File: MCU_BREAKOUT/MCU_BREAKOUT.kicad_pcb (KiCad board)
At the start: 4 copper layers, 15 parts, among them J1 Conn_01x06_Pin, J10 Conn_01x03_Pin, J2 Conn_01x02_Pin, J3 Conn_01x02_Pin, J4 Conn_01x04_Pin, J5 Conn_01x02_Pin, J6 Conn_01x02_Pin, J7 Conn_01x02_Pin, J8 Conn_01x03_Pin, J9 Conn_01x04_Pin, U1 ATMEGA168PA-MU, U2 XL7EL89CKI-111YLC-16M

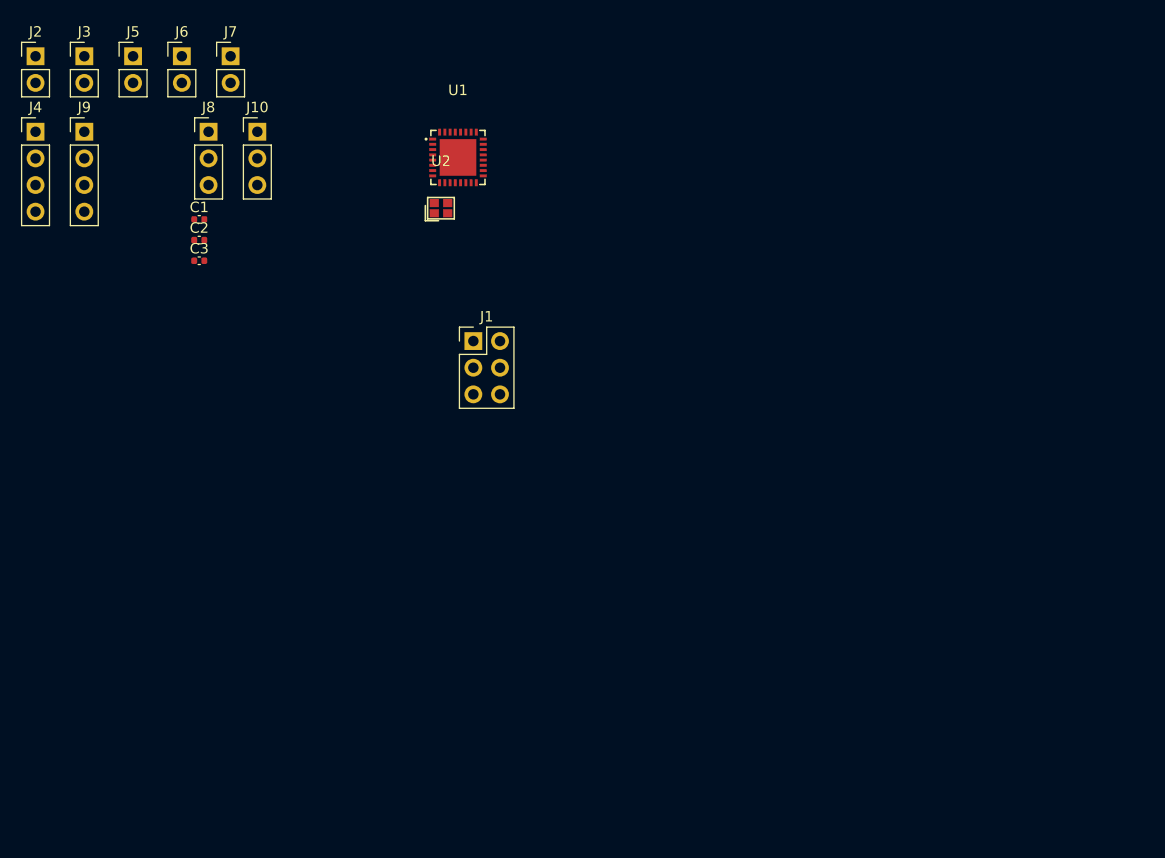
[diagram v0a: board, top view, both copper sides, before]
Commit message: RTC and GPS Breakouts Finished
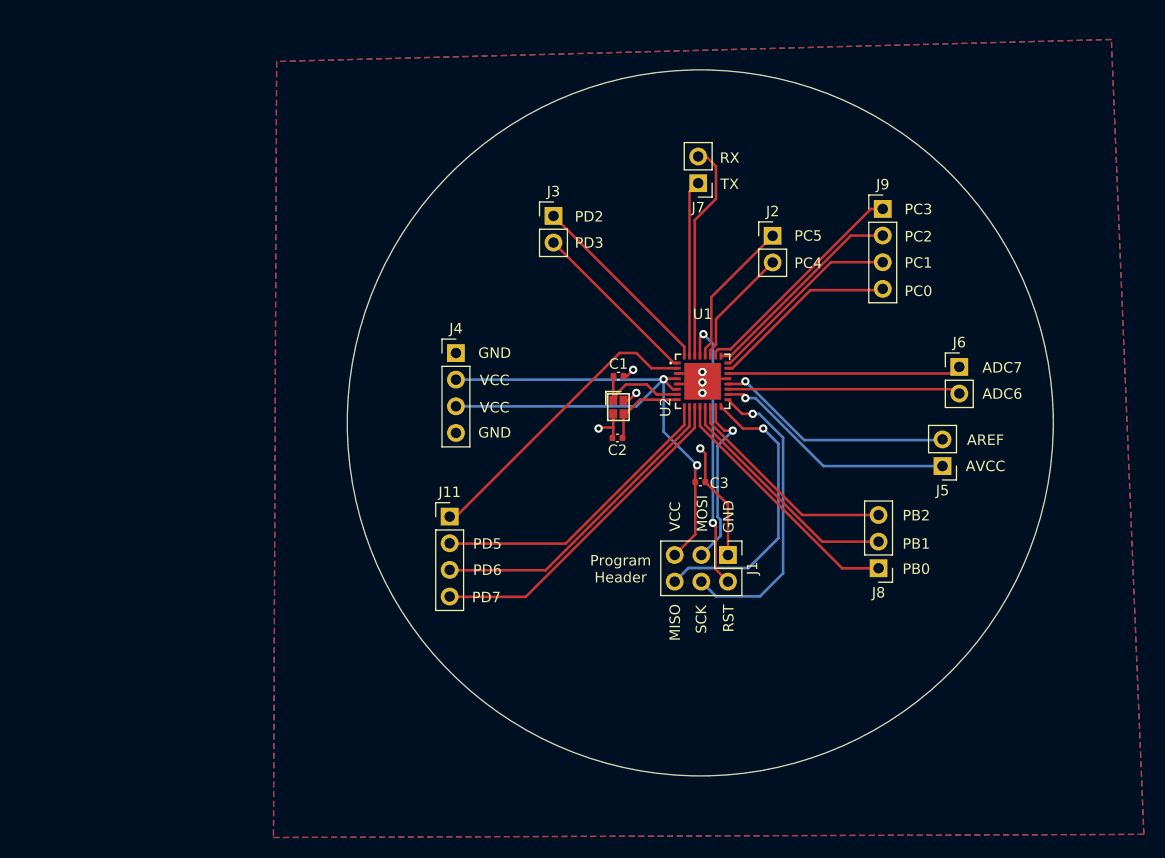
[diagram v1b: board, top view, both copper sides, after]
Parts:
- removed J10: Conn_01x03_Pin, Connector_PinHeader_2.54mm:PinHeader_1x03_P2.54mm_Vertical
- added J11: Conn_01x04_Pin, Connector_PinHeader_2.54mm:PinHeader_1x04_P2.54mm_Vertical, F.Cu at (143.0, 106.5)
- moved J5 86.5 mm to (190.0, 101.7), turned to 180 degrees
- moved J6 79.8 mm to (191.6, 92.2)
- moved J9 76.5 mm to (184.3, 77.2)
- moved J8 76.3 mm to (183.9, 111.4), turned to 180 degrees
- moved J2 72.3 mm to (173.8, 79.7)
- moved C3 52.2 mm to (166.9, 103.2), turned to 180 degrees
- moved J3 47.3 mm to (152.9, 77.8)
- moved J7 46.2 mm to (166.7, 74.7), turned to 180 degrees
- moved J4 45.3 mm to (143.6, 90.9)
- moved C2 44.1 mm to (159.0, 99.0), turned to 180 degrees
- moved C1 42.7 mm to (159.1, 93.1)
- moved J1 31.7 mm to (169.5, 110.2), turned to -90 degrees
- moved U1 31.6 mm to (167.1, 93.6)
- moved U2 25.4 mm to (159.1, 96.1), turned to -90 degrees
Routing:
- net VCC: track 0.00 -> 62.7 mm, vias 0 -> 2
- net /PD7: track 0.00 -> 32.1 mm
- net /PD6: track 0.00 -> 30.4 mm
- net /PB5: track 0.00 -> 29.0 mm, vias 0 -> 1
- net /PD5: track 0.00 -> 28.8 mm
- net /PD4: track 0.00 -> 28.8 mm
- net /PB4: track 0.00 -> 27.6 mm, vias 0 -> 1
- net /PC6: track 0.00 -> 26.8 mm, vias 0 -> 2
- net GND: track 0.00 -> 25.9 mm, vias 0 -> 7
- net /PB0: track 0.00 -> 24.5 mm
- net /AVCC: track 0.00 -> 23.6 mm, vias 0 -> 1
- net /AREF: track 0.00 -> 23.0 mm, vias 0 -> 1
- net /PB1: track 0.00 -> 22.9 mm
- net /ADC7: track 0.00 -> 22.3 mm
- net /ADC6: track 0.00 -> 22.2 mm
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- added copper zone on B.Cu, net GND
- added copper zone on F.Cu, net GND
- added copper zone on In1.Cu, net GND
- added copper zone on In2.Cu, net GND
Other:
- board outline added: 67.3 x 67.3 mm
- board text added: "ADC6"
- board text added: "ADC7"
- board text added: "AREF"
- board text added: "AVCC"
- board text added: "GND"
- board text added: "MISO"
- board text added: "MOSI"
- board text added: "PB0"
- board text added: "PB1"
- board text added: "PB2"
- board text added: "PC0"
- board text added: "PC1"
- board text added: "PC2"
- board text added: "PC3"
- board text added: "PC4"
- board text added: "PC5"
- board text added: "PD2"
- board text added: "PD3"
- board text added: "PD5"
- board text added: "PD6"
- board text added: "PD7"
- board text added: "Program Header"
- board text added: "RST"
- board text added: "RX"
- board text added: "SCK"
- board text added: "TX"
- board text added: "VCC"

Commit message: Added footprints and finished breakouts
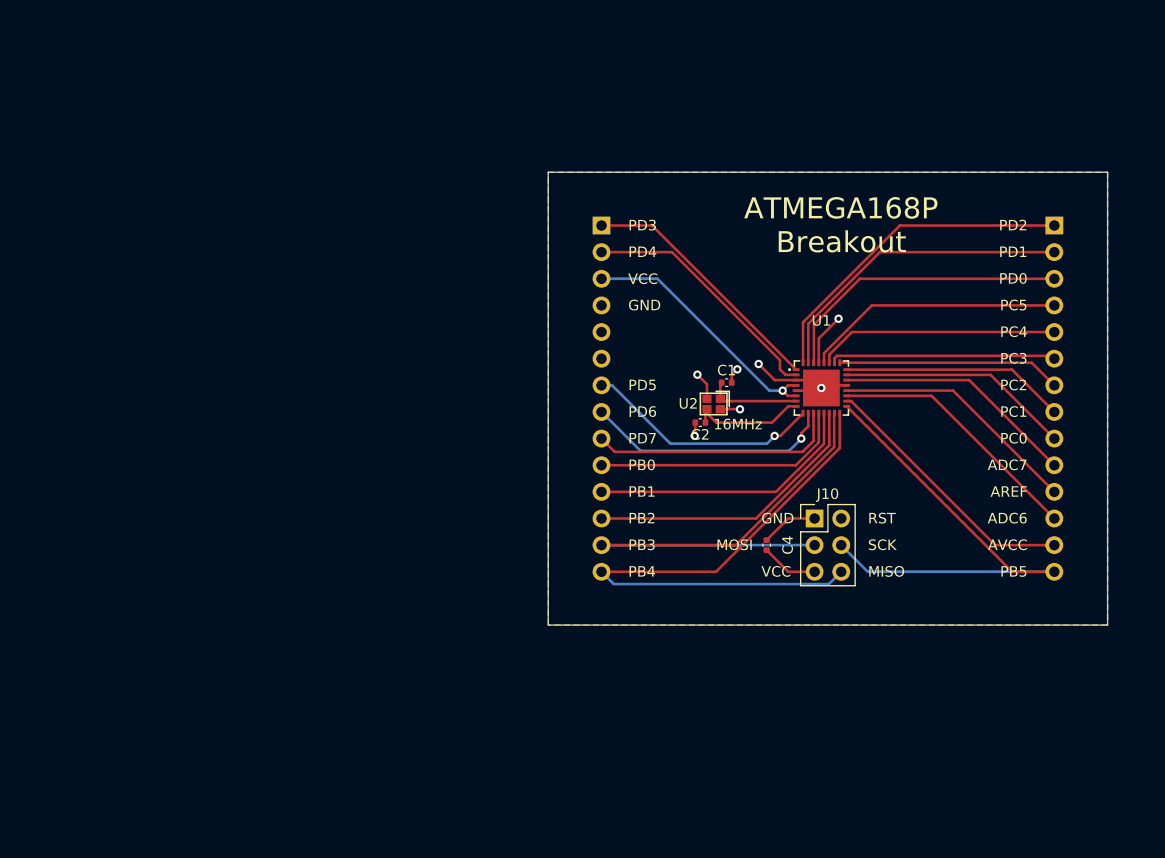
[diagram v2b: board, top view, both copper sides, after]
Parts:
- removed C3: 100n, Capacitor_SMD:C_0402_1005Metric
- removed J11, J4, J9: Conn_01x04_Pin, Connector_PinHeader_2.54mm:PinHeader_1x04_P2.54mm_Vertical
- removed J3, J5, J6, J7: Conn_01x02_Pin, Connector_PinHeader_2.54mm:PinHeader_1x02_P2.54mm_Vertical
- removed J8: Conn_01x03_Pin, Connector_PinHeader_2.54mm:PinHeader_1x03_P2.54mm_Vertical
- added C4: 100n, Capacitor_SMD:C_0402_1005Metric, F.Cu at (173.2, 109.2)
- added J10: Conn_01x06_Pin, Connector_PinHeader_2.54mm:PinHeader_2x03_P2.54mm_Vertical, F.Cu at (177.8, 106.7)
- J1: value Conn_01x06_Pin -> Conn_01x14_Pin; footprint Connector_PinHeader_2.54mm:PinHeader_2x03_P2.54mm_Vertical -> Connector_PinHeader_2.54mm:PinHeader_1x14_P2.54mm_Vertical; moved to B.Cu
- J2: value Conn_01x02_Pin -> Conn_01x14_Pin; footprint Connector_PinHeader_2.54mm:PinHeader_1x02_P2.54mm_Vertical -> Connector_PinHeader_2.54mm:PinHeader_1x14_P2.54mm_Vertical; moved to B.Cu
- moved J1 44.2 mm to (200.7, 78.7), turned to 180 degrees
- moved J2 16.3 mm to (157.5, 78.7), turned to 180 degrees
- moved U1 11.3 mm to (178.4, 94.2)
- moved C1 10.3 mm to (169.4, 93.7)
- moved U2 9.09 mm to (168.2, 95.8), turned to 180 degrees
- moved C2 8.04 mm to (166.9, 97.5)
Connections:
- J1 pad 1: GND -> /PD2
- J1 pad 2: /PC6 -> /PD1
- J1 pad 3: /PB3 -> /PD0
- J1 pad 4: /PB5 -> /PC5
- J1 pad 5: VCC -> /PC4
- J1 pad 6: /PB4 -> /PC3
- J2 pad 1: /PC5 -> /PD3
- J2 pad 2: /PC4 -> /PD4
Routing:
- net /PB3: track 16.8 -> 49.6 mm, vias 1 -> 0
- net /PB4: track 27.6 -> 54.8 mm, vias 1 -> 0
- net /PB5: track 29.0 -> 47.7 mm, vias 1 -> 0
- net VCC: track 62.7 -> 48.7 mm, vias 2 -> 1
- net /PD1: track 16.8 -> 30.0 mm
- net /PD2: track 18.5 -> 31.6 mm
- net /PC4: track 11.4 -> 23.1 mm
- net /PC5: track 14.1 -> 24.8 mm
- net /PD7: track 32.1 -> 23.8 mm
- net /PD3: track 16.6 -> 24.3 mm
- net /PD0: track 21.0 -> 28.4 mm
- net /PD6: track 30.4 -> 23.8 mm, vias 0 -> 1
- net /PB2: track 21.2 -> 27.7 mm
- net /PD5: track 28.8 -> 22.7 mm, vias 0 -> 1
- net /PD4: track 28.8 -> 23.9 mm
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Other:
- board size 67.3 x 67.3 mm -> 53.3 x 43.2 mm
- board text added: "16MHz"
- board text added: "ATMEGA168P Breakout"
- board text added: "PB3"
- board text added: "PB4"
- board text added: "PB5"
- board text added: "PD0"
- board text added: "PD1"
- board text added: "PD4"
- board text removed: "Program Header"
- board text removed: "RX"
- board text removed: "TX"
